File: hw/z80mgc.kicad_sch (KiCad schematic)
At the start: 8 parts, among them U1 Z80CPU, U10 74HC00, U2 28C256, U3 28C256, U4 71256, U5 74HC86, U8 74HC02, U9 74HC00

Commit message: Work on scmenatic and PCB
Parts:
- added C10, C3, C4, C5, C6, C7, C8, C9: Dec_Cap, Capacitor_THT:C_Disc_D3.0mm_W1.6mm_P2.50mm, symbol z80mgc:Dec_Cap
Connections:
- net +5V: now also U1.16 (~{INT}), U1.24 (~{WAIT}), U1.25 (~{BUSRQ}), C10.1, C3.1, C4.1, C5.1, C6.1, C7.1, C8.1, C9.1
- net ADDR10: now also U1.40 (A10); no longer U1.1 (A11)
- net ADDR11: now also U1.1 (A11); no longer U1.2 (A12)
- net ADDR12: now also U1.2 (A12); no longer U1.3 (A13)
- net ADDR13: now also U1.3 (A13); no longer U1.4 (A14)
- net ADDR14: now also U1.4 (A14); no longer U1.5 (A15)
- net ADDR15: now also U1.5 (A15)
- net ADDR7: no longer U1.38 (A8)
- net ADDR8: now also U1.38 (A8); no longer U1.39 (A9)
- net ADDR9: now also U1.39 (A9); no longer U1.40 (A10)
- net GND: now also C10.2, C3.2, C4.2, C5.2, C6.2, C7.2, C8.2, C9.2
- net ~{RESET}: now reaches U1.26 (~{RESET})
- net ~{CLK}: now reaches U1.6 (~{CLK})
- no-connect marks 6 -> 10
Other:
- moved on the sheet: U10E, U5E, U8E, U9E

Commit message: Work on scmenatic and PCB
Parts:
- removed C10, C7, C8, C9: Dec_Cap, Capacitor_THT:C_Disc_D3.0mm_W1.6mm_P2.50mm, symbol z80mgc:Dec_Cap
- removed U10, U9: 74HC00, Package_DIP:DIP-14_W7.62mm_Socket_LongPads, symbol 74xx:74HC00
- removed U5: 74HC86, Package_DIP:DIP-14_W7.62mm_Socket_LongPads, symbol 74xx:74HC86
- removed U8: 74HC02, Package_DIP:DIP-14_W7.62mm_Socket_LongPads, symbol 74xx:74HC02
- added U15: 74HC04, Package_DIP:DIP-14_W7.62mm_Socket_LongPads, symbol 74xx:74HC04
- added U16: 74HC00, Package_DIP:DIP-14_W7.62mm_Socket_LongPads, symbol 74xx:74HC00
- added U17: 74HC02, Package_DIP:DIP-14_W7.62mm_Socket_LongPads, symbol 74xx:74HC02
- C1: renamed from C5; value Dec_Cap -> 0.1uF
- CD1: renamed from C6; value Dec_Cap -> 0.1uF
- CD2: renamed from C3; value Dec_Cap -> 0.1uF
- CD3: renamed from C4; value Dec_Cap -> 0.1uF
- renumbered U1 to CPU1, U4 to U1, U2 to U5, U3 to U6
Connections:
- net ADDR14: now also U16.5, U17.5
- net ADDR15: now also U16.1, U17.3
- net ~{MREQ}: now also U15.5, U17.2
- net at U5.20 (~{CS}): now also U15.10
- net at U1.20 (~{CS}): now also U16.3
- net at U6.20 (~{CS}): now also U16.6
- new net: U15.9, U16.4, U17.1
- new net: U15.8, U17.6
- new net: U15.6, U16.2
- new net: U15.11, U17.4
- no-connect marks 10 -> 4

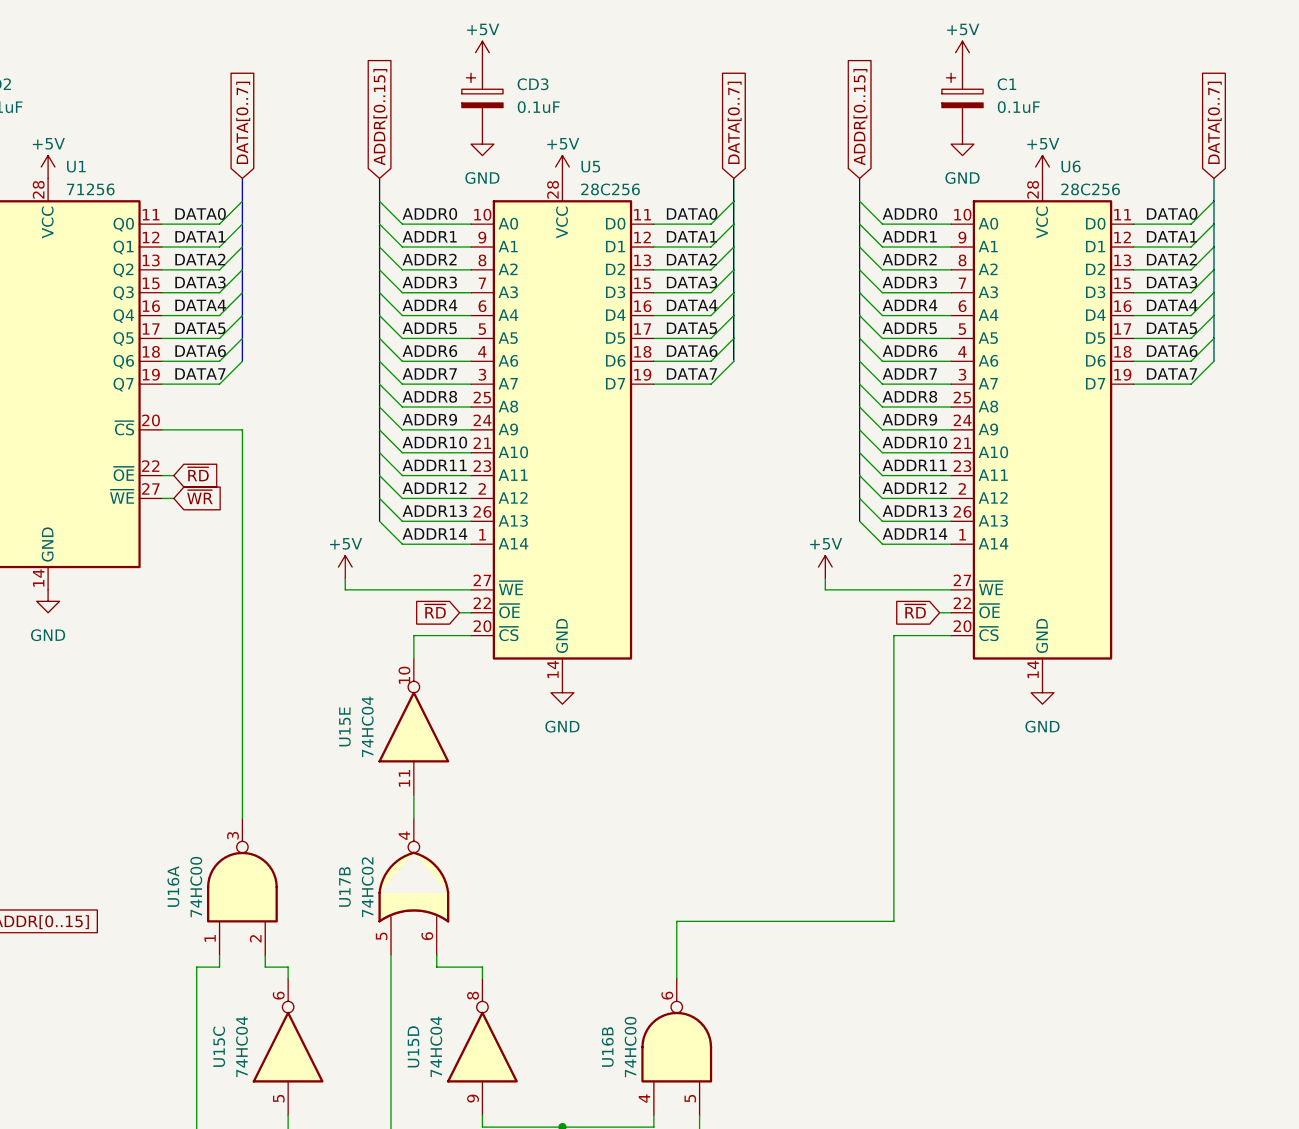
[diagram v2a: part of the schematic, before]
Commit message: Snake working with framebuffer
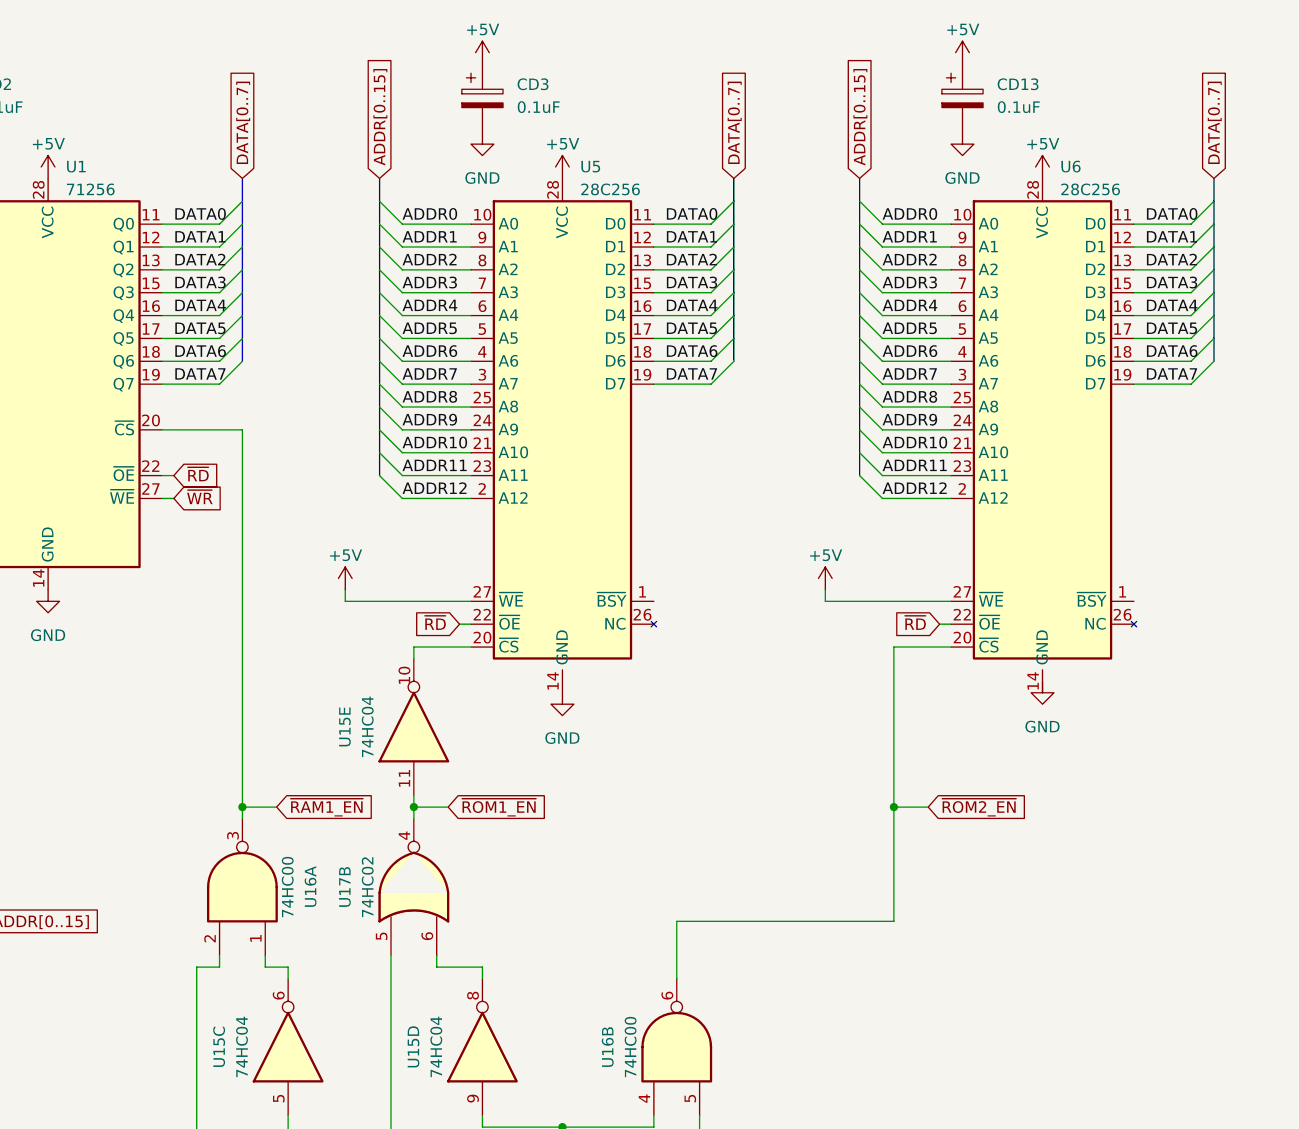
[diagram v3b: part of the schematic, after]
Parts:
- U5, U6: footprint Package_DIP:DIP-28_W15.24mm_Socket_LongPads -> Package_DIP:DIP-28_W15.24mm_LongPads; symbol Memory_EEPROM:28C256 -> z80mgc:28C65
- renumbered C1 to CD13
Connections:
- net ADDR13: no longer U5.26 (A13), U6.26 (A13)
- net ADDR14: no longer U5.1 (A14), U6.1 (A14)
- net ADDR15: now also U16.2; no longer U16.1
- net GND: no longer U6.14 (GND)
- net ~{RAM1_EN}: now reaches U1.20 (~{CS}), U16.3
- net ~{ROM2_EN}: now reaches U16.6, U6.20 (~{CS})
- net at U15.6: now also U16.1; no longer U16.2
- net ~{ROM1_EN}: now reaches U15.11, U17.4
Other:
- moved on the sheet: U16A

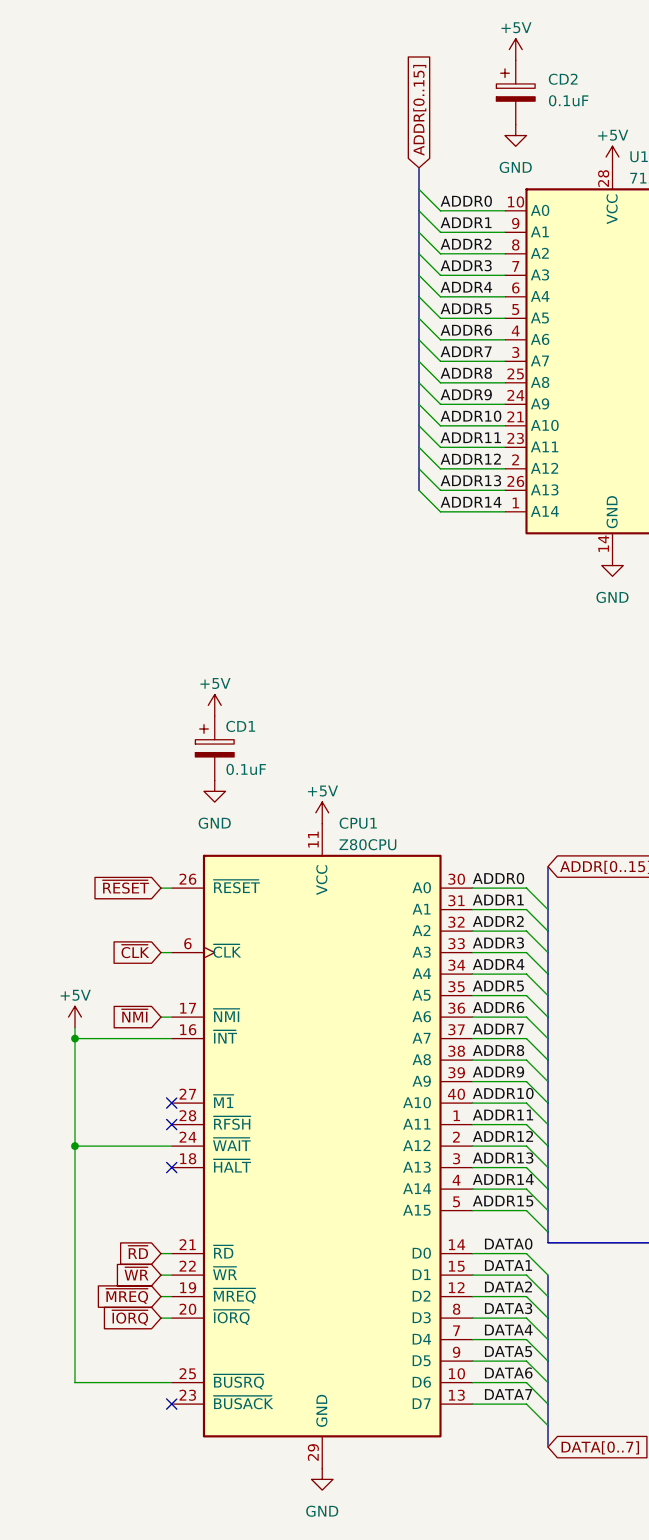
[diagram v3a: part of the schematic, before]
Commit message: Lots of work on Kicad, and gave up on PCB
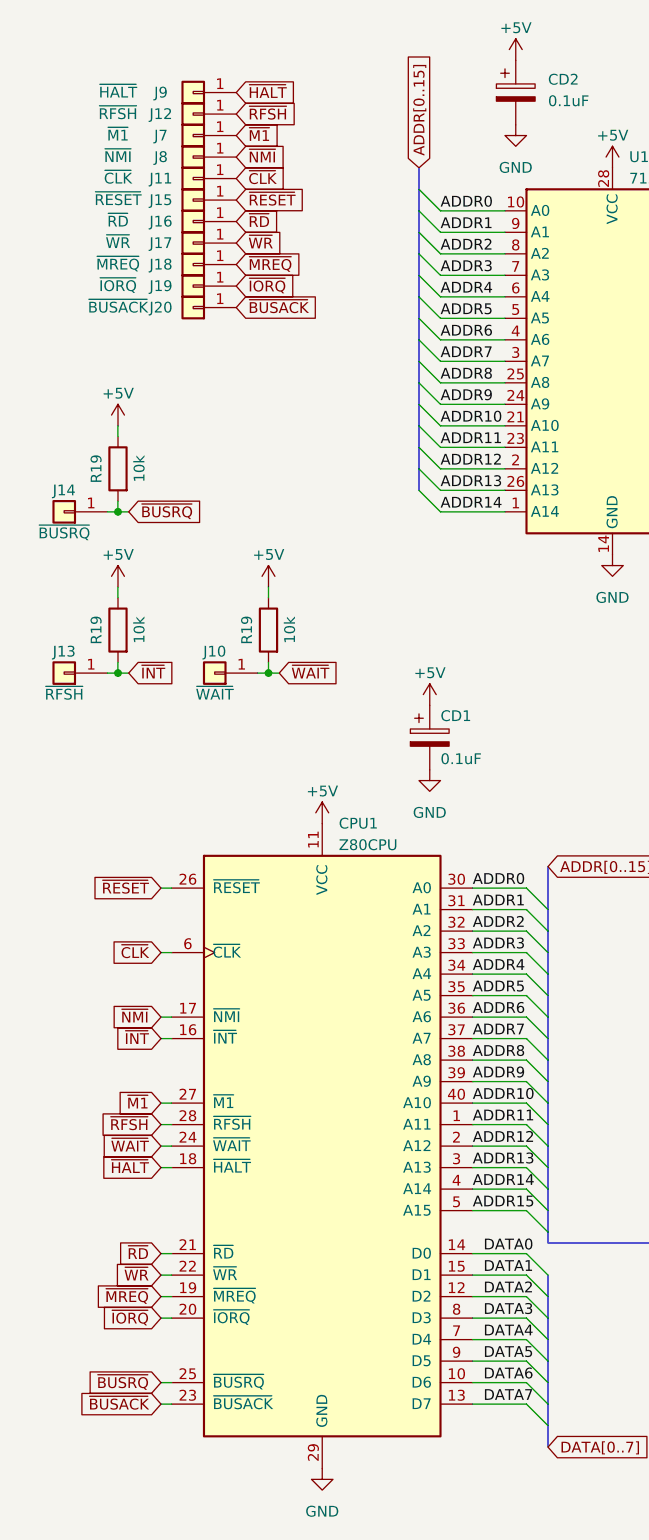
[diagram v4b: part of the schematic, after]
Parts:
- added J10: ~{WAIT}, Connector_PinHeader_1.27mm:PinHeader_1x01_P1.27mm_Vertical, symbol Connector_Generic:Conn_01x01
- added J11: ~{CLK}, Connector_PinHeader_1.27mm:PinHeader_1x01_P1.27mm_Vertical, symbol Connector_Generic:Conn_01x01
- added J12: ~{RFSH}, TestPoint:TestPoint_THTPad_D2.0mm_Drill1.0mm, symbol Connector_Generic:Conn_01x01
- added J13: ~{RFSH}, Connector_PinHeader_1.27mm:PinHeader_1x01_P1.27mm_Vertical, symbol Connector_Generic:Conn_01x01
- added J14: ~{BUSRQ}, Connector_PinHeader_1.27mm:PinHeader_1x01_P1.27mm_Vertical, symbol Connector_Generic:Conn_01x01
- added J15: ~{RESET}, Connector_PinHeader_1.27mm:PinHeader_1x01_P1.27mm_Vertical, symbol Connector_Generic:Conn_01x01
- added J16: ~{RD}, Connector_PinHeader_1.27mm:PinHeader_1x01_P1.27mm_Vertical, symbol Connector_Generic:Conn_01x01
- added J17: ~{WR}, Connector_PinHeader_1.27mm:PinHeader_1x01_P1.27mm_Vertical, symbol Connector_Generic:Conn_01x01
- added J18: ~{MREQ}, Connector_PinHeader_1.27mm:PinHeader_1x01_P1.27mm_Vertical, symbol Connector_Generic:Conn_01x01
- added J19: ~{IORQ}, Connector_PinHeader_1.27mm:PinHeader_1x01_P1.27mm_Vertical, symbol Connector_Generic:Conn_01x01
- added J20: ~{BUSACK}, Connector_PinHeader_1.27mm:PinHeader_1x01_P1.27mm_Vertical, symbol Connector_Generic:Conn_01x01
- added J7: ~{M1}, Connector_PinHeader_1.27mm:PinHeader_1x01_P1.27mm_Vertical, symbol Connector_Generic:Conn_01x01
- added J8: ~{NMI}, Connector_PinHeader_1.27mm:PinHeader_1x01_P1.27mm_Vertical, symbol Connector_Generic:Conn_01x01
- added J9: ~{HALT}, TestPoint:TestPoint_THTPad_D2.0mm_Drill1.0mm, symbol Connector_Generic:Conn_01x01
- added R19 (x3): 10k, Resistor_THT:R_Axial_DIN0207_L6.3mm_D2.5mm_P10.16mm_Horizontal, symbol z80mgc:Resistor
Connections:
- net +5V: now also R19.1, R19.1, R19.1; no longer CPU1.16 (~{INT}), CPU1.24 (~{WAIT}), CPU1.25 (~{BUSRQ})
- net ~{CLK}: now also J11.1 (Pin_1)
- net ~{IORQ}: now also J19.1 (Pin_1)
- net ~{MREQ}: now also J18.1 (Pin_1)
- net ~{NMI}: now also J8.1 (Pin_1)
- net ~{RD}: now also J16.1 (Pin_1)
- net ~{RESET}: now also J15.1 (Pin_1)
- net ~{WR}: now also J17.1 (Pin_1)
- net ~{HALT}: now reaches CPU1.18 (~{HALT})
- net ~{HALT}: now also J9.1 (Pin_1)
- net ~{BUSACK}: now reaches CPU1.23 (~{BUSACK})
- net ~{BUSACK}: now also J20.1 (Pin_1)
- net ~{M1}: now reaches CPU1.27 (~{M1})
- net ~{M1}: now also J7.1 (Pin_1)
- net ~{RFSH}: now reaches CPU1.28 (~{RFSH})
- net ~{RFSH}: now also J12.1 (Pin_1)
- new net ~{BUSRQ}: CPU1.25 (~{BUSRQ}), J14.1 (Pin_1), R19.2
- new net ~{INT}: CPU1.16 (~{INT}), J13.1 (Pin_1), R19.2
- new net ~{WAIT}: CPU1.24 (~{WAIT}), J10.1 (Pin_1), R19.2
- no-connect marks 4 -> 0
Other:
- moved on the sheet: CD1
